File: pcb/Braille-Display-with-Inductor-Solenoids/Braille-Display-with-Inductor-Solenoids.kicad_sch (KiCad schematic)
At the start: 25 parts, among them J1 Screw_Terminal_01x02, J2 Screw_Terminal_01x02, J3 Screw_Terminal_01x02, J4 Conn_01x03, J5 Conn_01x02, J6 Conn_01x08, SW1 SW_Push, SW2 SW_Push, U1 RP2040-Zero

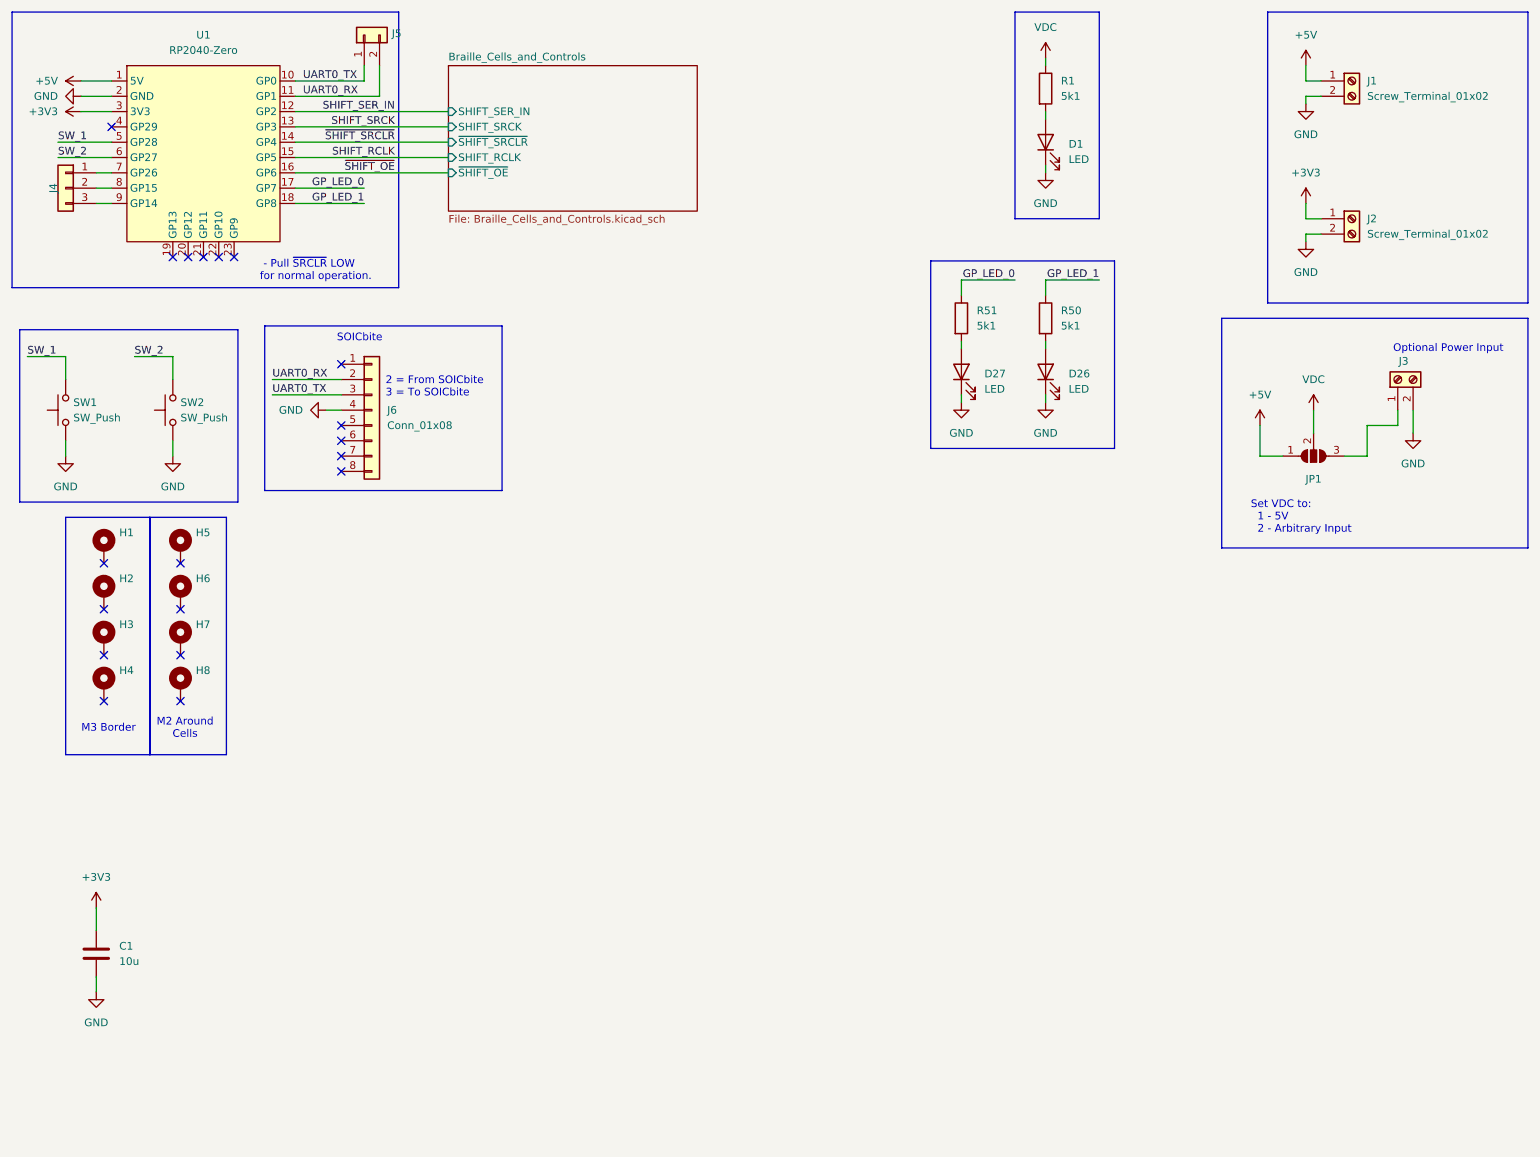
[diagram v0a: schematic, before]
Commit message: PCB (Rev 3): Switch to 2 inductors per cell (#2)
* WIP (Rev3): Switch to 2 inductors per cell

* WIP: Route one cell

* WIP: Route more of the board

* WIP: Swap around power input placement

* Finish and polish design

* Bit of tiny routing, export production file
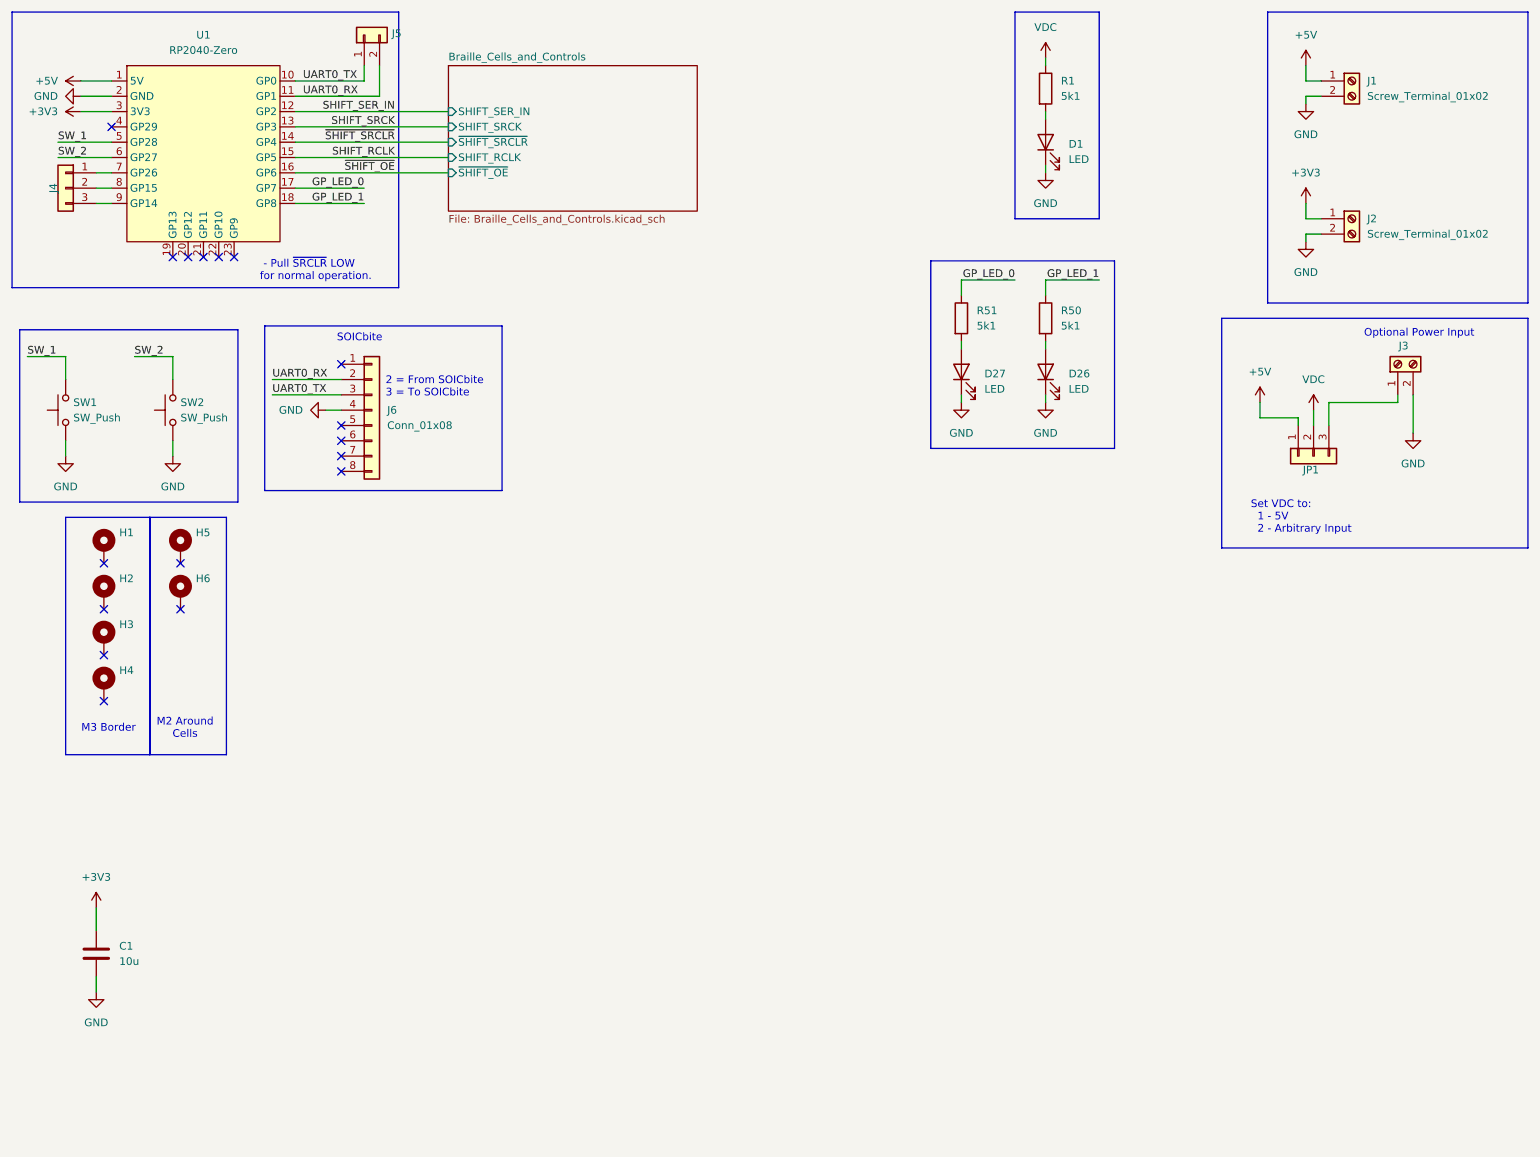
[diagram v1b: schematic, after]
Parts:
- removed H7, H8: MountingHole_Pad, 00-project-footprints:Braille_Block_MountingHoles_M2_3x, symbol Mechanical:MountingHole_Pad
- D1, D26, D27: footprint LED_SMD:LED_1206_3216Metric_Pad1.42x1.75mm_HandSolder -> LED_SMD:LED_0603_1608Metric_Pad1.05x0.95mm_HandSolder
- JP1: symbol Jumper:SolderJumper_3_Open -> Connector_Generic:Conn_01x03; now in the parts list
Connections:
- no-connect marks 19 -> 17
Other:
- moved on the sheet: J3
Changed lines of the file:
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@@
 	(paper "USLetter")
 	(title_block
-		(date "2024-11-27")
-		(rev "Rev 2")
+		(date "2025-01-05")
+		(rev "Rev 3")
 	)
 	(no_connect
@@
 	)
 	(no_connect
-		(at 41.91 128.27)
-	)
-	(no_connect
 		(at 43.18 54.61)
 	)
@@
 	)
 	(no_connect
-		(at 41.91 120.65)
-	)
-	(no_connect
 		(at 68.58 90.17)
 	)
@@
 	(wire
 		(pts
-			(xy 246.38 83.82) (xy 246.38 80.01)
+			(xy 246.38 83.82) (xy 246.38 77.47)
 		)
 		(stroke
@@
 	(wire
 		(pts
+			(xy 220.98 81.28) (xy 220.98 78.74)
+		)
+		(stroke
+			(width 0)
+			(type default)
+		)
+	)
+	(wire
+		(pts
 			(xy 185.42 77.47) (xy 185.42 78.74)
 		)
@@
 	(wire
 		(pts
-			(xy 229.87 80.01) (xy 229.87 83.82)
-		)
-		(stroke
-			(width 0)
-			(type default)
-		)
-	)
-	(wire
-		(pts
-			(xy 238.76 87.63) (xy 238.76 82.55)
-		)
-		(stroke
-			(width 0)
-			(type default)
-		)
-	)
-	(wire
-		(pts
-			(xy 243.84 82.55) (xy 243.84 80.01)
+			(xy 232.41 82.55) (xy 232.41 78.74)
 		)
 		(stroke
@@
 	(wire
 		(pts
-			(xy 238.76 82.55) (xy 243.84 82.55)
+			(xy 232.41 78.74) (xy 243.84 78.74)
 		)
 		(stroke
@@
 	(wire
 		(pts
-			(xy 220.98 87.63) (xy 224.79 87.63)
+			(xy 243.84 78.74) (xy 243.84 77.47)
 		)
 		(stroke
@@
 	(wire
 		(pts
-			(xy 220.98 82.55) (xy 220.98 87.63)
+			(xy 229.87 80.01) (xy 229.87 82.55)
 		)
 		(stroke
@@
 	(wire
 		(pts
+			(xy 227.33 81.28) (xy 227.33 82.55)
+		)
+		(stroke
+			(width 0)
+			(type default)
+		)
+	)
+	(wire
+		(pts
 			(xy 228.6 50.8) (xy 231.14 50.8)
 		)
@@
 	(wire
 		(pts
-			(xy 57.15 74.93) (xy 68.58 74.93)
+			(xy 220.98 81.28) (xy 227.33 81.28)
 		)
 		(stroke
@@
 	(wire
 		(pts
-			(xy 234.95 87.63) (xy 238.76 87.63)
+			(xy 57.15 74.93) (xy 68.58 74.93)
 		)
 		(stroke
@@
 	(text "Optional Power Input"
 		(exclude_from_sim no)
-		(at 252.222 69.85 0)
+		(at 247.396 67.31 0)
 		(effects
 			(font
@@
 		(length 2.54)
 		(shape round)
-		(at 236.22 87.63 180)
+		(at 234.95 78.74 0)
 		(fields_autoplaced yes)
 		(effects
@@
 				(size 1.27 1.27)
 			)
-			(justify right bottom)
+			(justify left bottom)
 		)
 		(property "Netclass" "Power"
-			(at 236.9185 90.17 0)
+			(at 235.6485 76.2 0)
 			(effects
 				(font
@@
 			)
 		)
-		(property "Footprint" "LED_SMD:LED_1206_3216Metric_Pad1.42x1.75mm_HandSolder"
+		(property "Footprint" "LED_SMD:LED_0603_1608Metric_Pad1.05x0.95mm_HandSolder"
 			(at 171.45 73.66 0)
 			(effects
@@
 			)
 		)
-		(property "Footprint" "LED_SMD:LED_1206_3216Metric_Pad1.42x1.75mm_HandSolder"
+		(property "Footprint" "LED_SMD:LED_0603_1608Metric_Pad1.05x0.95mm_HandSolder"
 			(at 185.42 73.66 0)
 			(effects
@@
 	(symbol
 		(lib_id "Connector:Screw_Terminal_01x02")
-		(at 243.84 74.93 90)
+		(at 243.84 72.39 90)
 		(unit 1)
 		(exclude_from_sim no)
@@
 		(dnp no)
 		(property "Reference" "J3"
-			(at 245.618 71.882 90)
+			(at 245.618 69.342 90)
 			(effects
 				(font
@@
 		)
 		(property "Value" "Screw_Terminal_01x02"
-			(at 246.3799 72.39 90)
+			(at 246.3799 69.85 90)
 			(effects
 				(font
@@
 		)
 		(property "Footprint" "TerminalBlock:TerminalBlock_bornier-2_P5.08mm"
-			(at 243.84 74.93 0)
+			(at 243.84 72.39 0)
 			(effects
 				(font
@@
 		)
 		(property "Datasheet" "~"
-			(at 243.84 74.93 0)
+			(at 243.84 72.39 0)
 			(effects
 				(font
@@
 		)
 		(property "Description" "Generic screw terminal, single row, 01x02, script generated (kicad-library-utils/schlib/autogen/connector/)"
-			(at 243.84 74.93 0)
+			(at 243.84 72.39 0)
 			(effects
 				(font
@@
 	(symbol
 		(lib_id "power:+5V")
-		(at 220.98 82.55 0)
+		(at 220.98 78.74 0)
 		(mirror y)
 		(unit 1)
@@
 		(fields_autoplaced yes)
 		(property "Reference" "#PWR010"
-			(at 220.98 86.36 0)
+			(at 220.98 82.55 0)
 			(effects
 				(font
@@
 		)
 		(property "Value" "+5V"
-			(at 220.98 77.47 0)
+			(at 220.98 73.66 0)
 			(effects
 				(font
@@
 		)
 		(property "Footprint" ""
-			(at 220.98 82.55 0)
+			(at 220.98 78.74 0)
 			(effects
 				(font
@@
 		)
 		(property "Datasheet" ""
-			(at 220.98 82.55 0)
+			(at 220.98 78.74 0)
 			(effects
 				(font
@@
 		)
 		(property "Description" "Power symbol creates a global label with name \"+5V\""
-			(at 220.98 82.55 0)
+			(at 220.98 78.74 0)
 			(effects
 				(font
@@
 	)
 	(symbol
-		(lib_id "Mechanical:MountingHole_Pad")
-		(at 41.91 125.73 0)
-		(unit 1)
-		(exclude_from_sim yes)
-		(in_bom no)
-		(on_board yes)
-		(dnp no)
-		(fields_autoplaced yes)
-		(property "Reference" "H8"
-			(at 44.45 123.1899 0)
-			(effects
-				(font
-					(size 1.27 1.27)
-				)
-				(justify left)
-			)
-		)
-		(property "Value" "MountingHole_Pad"
-			(at 44.45 125.7299 0)
-			(effects
-				(font
-					(size 1.27 1.27)
-				)
-				(justify left)
-				(hide yes)
-			)
-		)
-		(property "Footprint" "00-project-footprints:Braille_Block_MountingHoles_M2_3x"
-			(at 41.91 125.73 0)
-			(effects
-				(font
-					(size 1.27 1.27)
-				)
-				(hide yes)
-			)
-		)
-		(property "Datasheet" "~"
-			(at 41.91 125.73 0)
-			(effects
-				(font
-					(size 1.27 1.27)
-				)
-				(hide yes)
-			)
-		)
-		(property "Description" "Mounting Hole with connection"
-			(at 41.91 125.73 0)
-			(effects
-				(font
-					(size 1.27 1.27)
-				)
-				(hide yes)
-			)
-		)
-		(pin "1"
-		)
-		(instances
-			(project "Braille-Display-with-Inductor-Solenoids"
-				(path "/3829a125-89bd-48f9-bfbe-92d753eb8f7f"
-					(reference "H8")
-					(unit 1)
-				)
-			)
-		)
-	)
-	(symbol
-		(lib_id "Mechanical:MountingHole_Pad")
-		(at 41.91 118.11 0)
-		(unit 1)
-		(exclude_from_sim yes)
-		(in_bom no)
-		(on_board yes)
-		(dnp no)
-		(fields_autoplaced yes)
-		(property "Reference" "H7"
-			(at 44.45 115.5699 0)
-			(effects
-				(font
-					(size 1.27 1.27)
-				)
-				(justify left)
-			)
-		)
-		(property "Value" "MountingHole_Pad"
-			(at 44.45 118.1099 0)
-			(effects
-				(font
-					(size 1.27 1.27)
-				)
-				(justify left)
-				(hide yes)
-			)
-		)
-		(property "Footprint" "00-project-footprints:Braille_Block_MountingHoles_M2_3x"
-			(at 41.91 118.11 0)
-			(effects
-				(font
-					(size 1.27 1.27)
-				)
-				(hide yes)
-			)
-		)
-		(property "Datasheet" "~"
-			(at 41.91 118.11 0)
-			(effects
-				(font
-					(size 1.27 1.27)
-				)
-				(hide yes)
-			)
-		)
-		(property "Description" "Mounting Hole with connection"
-			(at 41.91 118.11 0)
-			(effects
-				(font
-					(size 1.27 1.27)
-				)
-				(hide yes)
-			)
-		)
-		(pin "1"
-		)
-		(instances
-			(project "Braille-Display-with-Inductor-Solenoids"
-				(path "/3829a125-89bd-48f9-bfbe-92d753eb8f7f"
-					(reference "H7")
-					(unit 1)
-				)
-			)
-		)
-	)
-	(symbol
 		(lib_id "power:VDC")
 		(at 229.87 80.01 0)
@@
 			)
 		)
-		(property "Footprint" "LED_SMD:LED_1206_3216Metric_Pad1.42x1.75mm_HandSolder"
+		(property "Footprint" "LED_SMD:LED_0603_1608Metric_Pad1.05x0.95mm_HandSolder"
 			(at 185.42 35.56 0)
 			(effects
@@
 	)
 	(symbol
-		(lib_id "Jumper:SolderJumper_3_Open")
-		(at 229.87 87.63 0)
+		(lib_id "Connector_Generic:Conn_01x03")
+		(at 229.87 87.63 90)
 		(mirror x)
 		(unit 1)
-		(exclude_from_sim yes)
-		(in_bom no)
+		(exclude_from_sim no)
+		(in_bom yes)
 		(on_board yes)
 		(dnp no)
-		(fields_autoplaced yes)
 		(property "Reference" "JP1"
-			(at 229.87 91.44 0)
+			(at 228.092 89.916 90)
 			(effects
 				(font
 					(size 1.27 1.27)
 				)
+				(justify right)
 			)
 		)
 		(property "Value" "SolderJumper_3_Open"
-			(at 229.87 93.98 0)
+			(at 223.52 87.63 0)
 			(effects
 				(font
@@
 			)
 		)
-		(property "Description" "Solder Jumper, 3-pole, open"
+		(property "Description" "Generic connector, single row, 01x03, script generated (kicad-library-utils/schlib/autogen/connector/)"
 			(at 229.87 87.63 0)
 			(effects
